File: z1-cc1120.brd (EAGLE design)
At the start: 100 x 50 mm, 13 parts, among them X1 PN61729-S

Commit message: added CCA_STATUS
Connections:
- new net RADIO_CCA_STATUS: U$1.C42, U$2.GPIO3
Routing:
- net RADIO_CCA_STATUS: track 0.00 -> 80.4 mm, vias 0 -> 1
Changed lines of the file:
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@@
 <signal name="N$2">
+</signal>
+<signal name="RADIO_CCA_STATUS">
+<contactref element="U$2" pad="GPIO3"/>
+<contactref element="U$1" pad="C42"/>
+<wire x1="96.774" y1="18.415" x2="98.679" y2="18.415" width="0.4064" layer="1"/>
+<wire x1="98.679" y1="18.415" x2="99.187" y2="17.907" width="0.4064" layer="1"/>
+<wire x1="99.187" y1="17.907" x2="99.187" y2="9.144" width="0.4064" layer="1"/>
+<wire x1="99.187" y1="9.144" x2="98.171" y2="8.128" width="0.4064" layer="1"/>
+<wire x1="98.171" y1="8.128" x2="48.133" y2="8.128" width="0.4064" layer="1"/>
+<wire x1="48.133" y1="8.128" x2="47.244" y2="9.017" width="0.4064" layer="1"/>
+<via x="47.244" y="9.017" extent="1-16" drill="0.4826"/>
+<wire x1="47.244" y1="9.017" x2="46.228" y2="10.033" width="0.4064" layer="16"/>
+<wire x1="46.228" y1="10.033" x2="39.497" y2="10.033" width="0.4064" layer="16"/>
+<wire x1="39.497" y1="10.033" x2="36.83" y2="12.7" width="0.4064" layer="16"/>
+<wire x1="36.83" y1="12.7" x2="36.83" y2="17.018" width="0.4064" layer="16"/>
 </signal>
 </signals>

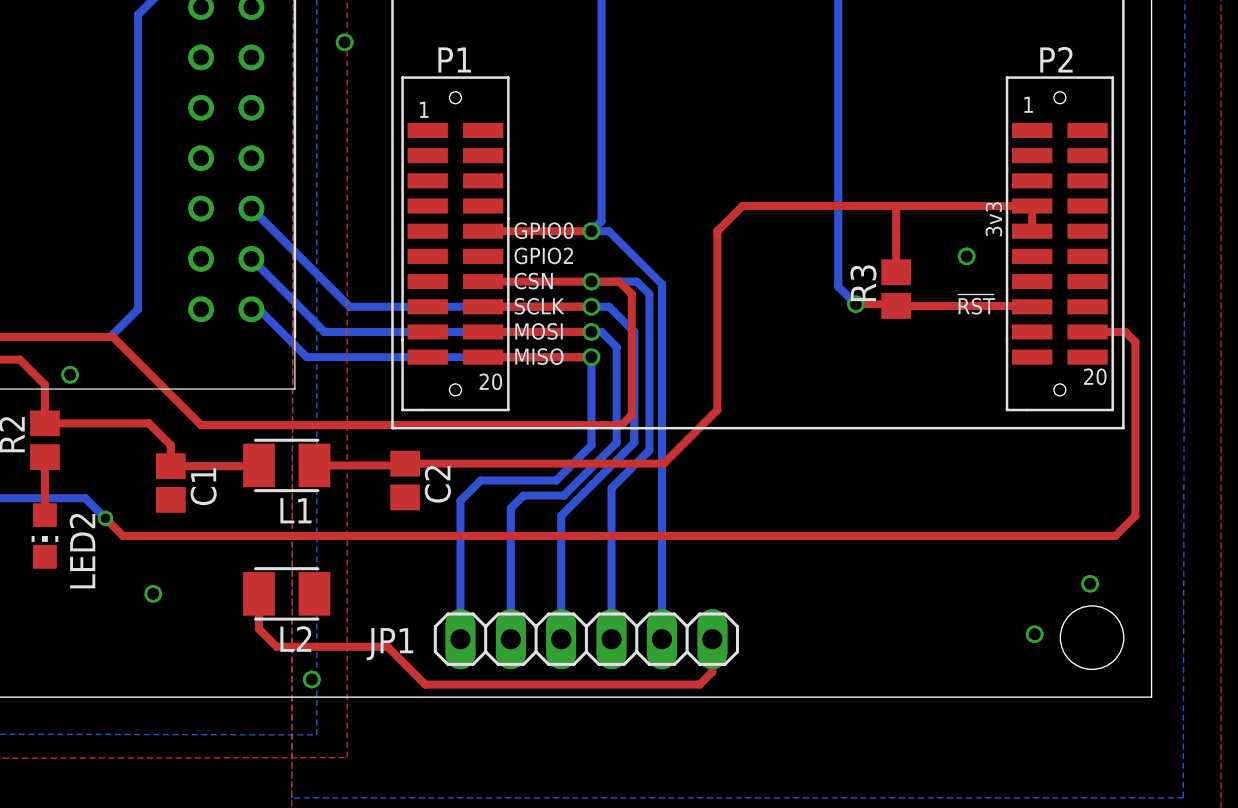
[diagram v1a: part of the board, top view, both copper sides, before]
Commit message: added !rst and cca status onto debug header
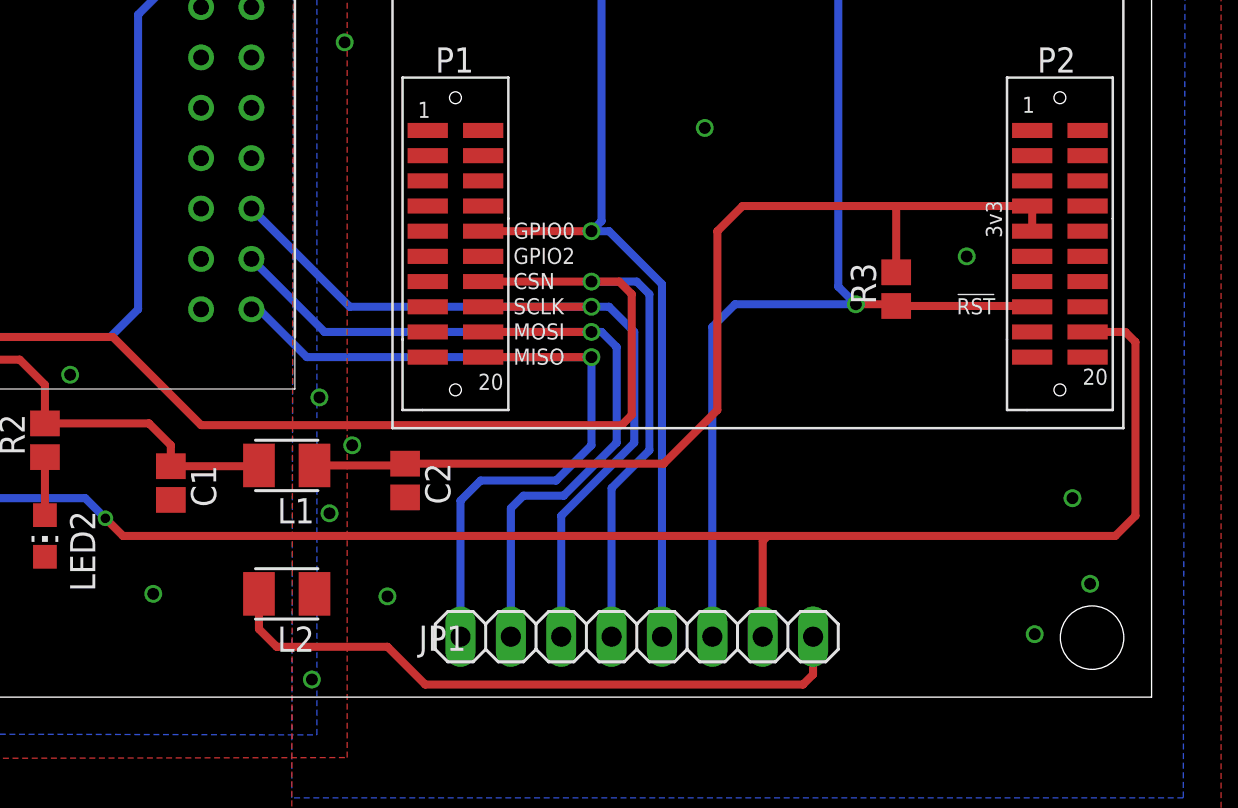
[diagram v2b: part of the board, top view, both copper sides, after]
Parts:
- JP1: device pinhead:1X06 -> pinhead:1X08
- moved JP1 2.54 mm to (74.0, 3.05)
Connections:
- net GND: now also JP1.8; no longer JP1.6
- net RADIO_!RST: now also JP1.6
- net RADIO_CCA_STATUS: now also JP1.7
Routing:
- net RADIO_!RST: track 94.9 -> 118.2 mm
- net GND: track 27.7 -> 33.0 mm
- net RADIO_CCA_STATUS: track 80.4 -> 85.6 mm
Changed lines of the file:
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@@
 <element name="L1" library="resistor" package="L3230M" value="10mH" x="56.388" y="11.684" rot="R180"/>
 <element name="L2" library="resistor" package="L3230M" value="10mH" x="56.388" y="5.207" rot="R180"/>
-<element name="JP1" library="pinhead" package="1X06" value="" x="71.501" y="2.921" smashed="yes">
-<attribute name="NAME" x="60.5028" y="2.2098" size="1.27" layer="25" ratio="10"/>
-<attribute name="VALUE" x="63.881" y="-0.254" size="1.27" layer="27"/>
+<element name="JP1" library="pinhead" package="1X08" value="" x="74.041" y="3.048" smashed="yes">
+<attribute name="NAME" x="63.0428" y="2.3368" size="1.27" layer="25" ratio="10"/>
+<attribute name="VALUE" x="66.421" y="-0.127" size="1.27" layer="27"/>
 </element>
 <element name="R3" library="resistor" package="R0805" value="1K" x="87.122" y="20.574" rot="R90"/>
@@
 <contactref element="L2" pad="2"/>
 <via x="45.466" y="16.256" extent="1-16" drill="0.6" shape="octagon"/>
-<contactref element="JP1" pad="6"/>
 <wire x1="54.988" y1="5.207" x2="54.988" y2="3.432" width="0.4064" layer="1"/>
 <wire x1="54.988" y1="3.432" x2="55.88" y2="2.54" width="0.4064" layer="1"/>
 <wire x1="55.88" y1="2.54" x2="61.468" y2="2.54" width="0.4064" layer="1"/>
 <wire x1="61.468" y1="2.54" x2="63.373" y2="0.635" width="0.4064" layer="1"/>
-<wire x1="63.373" y1="0.635" x2="77.216" y2="0.635" width="0.4064" layer="1"/>
-<wire x1="77.216" y1="0.635" x2="77.851" y2="1.27" width="0.4064" layer="1"/>
-<wire x1="77.851" y1="1.27" x2="77.851" y2="2.921" width="0.4064" layer="1"/>
+<wire x1="63.373" y1="0.635" x2="82.423" y2="0.635" width="0.4064" layer="1"/>
 <via x="49.657" y="5.207" extent="1-16" drill="0.6" shape="octagon"/>
+<contactref element="JP1" pad="8"/>
+<wire x1="82.423" y1="0.635" x2="82.931" y2="1.143" width="0.4064" layer="1"/>
+<wire x1="82.931" y1="1.143" x2="82.931" y2="3.048" width="0.4064" layer="1"/>
 </signal>
 <signal name="VCC_3V3">
@@
 <wire x1="73.914" y1="18.415" x2="73.914" y2="12.827" width="0.4064" layer="16"/>
 <wire x1="73.914" y1="12.827" x2="70.231" y2="9.144" width="0.4064" layer="16"/>
-<wire x1="70.231" y1="9.144" x2="70.231" y2="2.921" width="0.4064" layer="16"/>
+<wire x1="70.231" y1="9.144" x2="70.231" y2="3.048" width="0.4064" layer="16"/>
 </signal>
 <signal name="SPI_SIMO">
@@
 <wire x1="70.358" y1="10.16" x2="68.326" y2="10.16" width="0.4064" layer="16"/>
 <wire x1="68.326" y1="10.16" x2="67.691" y2="9.525" width="0.4064" layer="16"/>
-<wire x1="67.691" y1="9.525" x2="67.691" y2="2.921" width="0.4064" layer="16"/>
+<wire x1="67.691" y1="9.525" x2="67.691" y2="3.048" width="0.4064" layer="16"/>
 </signal>
 <signal name="SPI_SOMI">
@@
 <wire x1="69.977" y1="10.922" x2="66.167" y2="10.922" width="0.4064" layer="16"/>
 <wire x1="66.167" y1="10.922" x2="65.151" y2="9.906" width="0.4064" layer="16"/>
-<wire x1="65.151" y1="9.906" x2="65.151" y2="2.921" width="0.4064" layer="16"/>
+<wire x1="65.151" y1="9.906" x2="65.151" y2="3.048" width="0.4064" layer="16"/>
 </signal>
 <signal name="RADIO_CSN">
@@
 <wire x1="52.07" y1="13.716" x2="47.625" y2="18.161" width="0.4064" layer="1"/>
 <contactref element="JP1" pad="4"/>
-<wire x1="72.771" y1="2.921" x2="72.771" y2="10.541" width="0.4064" layer="16"/>
+<wire x1="72.771" y1="3.048" x2="72.771" y2="10.541" width="0.4064" layer="16"/>
 <wire x1="72.771" y1="10.541" x2="74.676" y2="12.446" width="0.4064" layer="16"/>
 <wire x1="74.676" y1="12.446" x2="74.676" y2="20.32" width="0.4064" layer="16"/>
@@
 <wire x1="71.755" y1="23.495" x2="72.644" y2="23.495" width="0.4064" layer="16"/>
 <wire x1="72.644" y1="23.495" x2="75.311" y2="20.828" width="0.4064" layer="16"/>
-<wire x1="75.311" y1="20.828" x2="75.311" y2="2.921" width="0.4064" layer="16"/>
+<wire x1="75.311" y1="20.828" x2="75.311" y2="3.048" width="0.4064" layer="16"/>
 <contactref element="U$1" pad="C54"/>
 <wire x1="47.498" y1="18.161" x2="22.733" y2="18.161" width="0.4064" layer="16"/>
@@
 <via x="59.309" y="33.02" extent="1-16" drill="0.6"/>
 <via x="90.678" y="22.225" extent="1-16" drill="0.6"/>
+<via x="61.468" y="5.08" extent="1-16" drill="0.6" shape="octagon"/>
+<via x="96.012" y="10.033" extent="1-16" drill="0.6" shape="octagon"/>
+<via x="58.547" y="9.271" extent="1-16" drill="0.6" shape="octagon"/>
+<via x="58.039" y="15.113" extent="1-16" drill="0.6" shape="octagon"/>
+<via x="59.69" y="12.7" extent="1-16" drill="0.6" shape="octagon"/>
+<via x="77.47" y="28.702" extent="1-16" drill="0.6" shape="octagon"/>
 </signal>
 <signal name="RADIO_3V3">
@@
 <wire x1="87.122" y1="19.724" x2="87.034" y2="19.724" width="0.4064" layer="1"/>
 <wire x1="87.034" y1="19.724" x2="87.034" y2="19.812" width="0.4064" layer="1"/>
+<contactref element="JP1" pad="6"/>
+<wire x1="85.09" y1="19.812" x2="78.994" y2="19.812" width="0.4064" layer="16"/>
+<wire x1="78.994" y1="19.812" x2="77.851" y2="18.669" width="0.4064" layer="16"/>
+<wire x1="77.851" y1="18.669" x2="77.851" y2="3.048" width="0.4064" layer="16"/>
 </signal>
 <signal name="N$2">
@@
 <wire x1="99.187" y1="17.907" x2="99.187" y2="9.144" width="0.4064" layer="1"/>
 <wire x1="99.187" y1="9.144" x2="98.171" y2="8.128" width="0.4064" layer="1"/>
-<wire x1="98.171" y1="8.128" x2="48.133" y2="8.128" width="0.4064" layer="1"/>
+<wire x1="98.171" y1="8.128" x2="80.645" y2="8.128" width="0.4064" layer="1"/>
+<wire x1="80.645" y1="8.128" x2="48.133" y2="8.128" width="0.4064" layer="1"/>
 <wire x1="48.133" y1="8.128" x2="47.244" y2="9.017" width="0.4064" layer="1"/>
 <via x="47.244" y="9.017" extent="1-16" drill="0.4826"/>
@@
 <wire x1="39.497" y1="10.033" x2="36.83" y2="12.7" width="0.4064" layer="16"/>
 <wire x1="36.83" y1="12.7" x2="36.83" y2="17.018" width="0.4064" layer="16"/>
+<contactref element="JP1" pad="7"/>
+<wire x1="80.391" y1="3.048" x2="80.391" y2="7.874" width="0.4064" layer="1"/>
+<wire x1="80.391" y1="7.874" x2="80.645" y2="8.128" width="0.4064" layer="1"/>
 </signal>
 </signals>

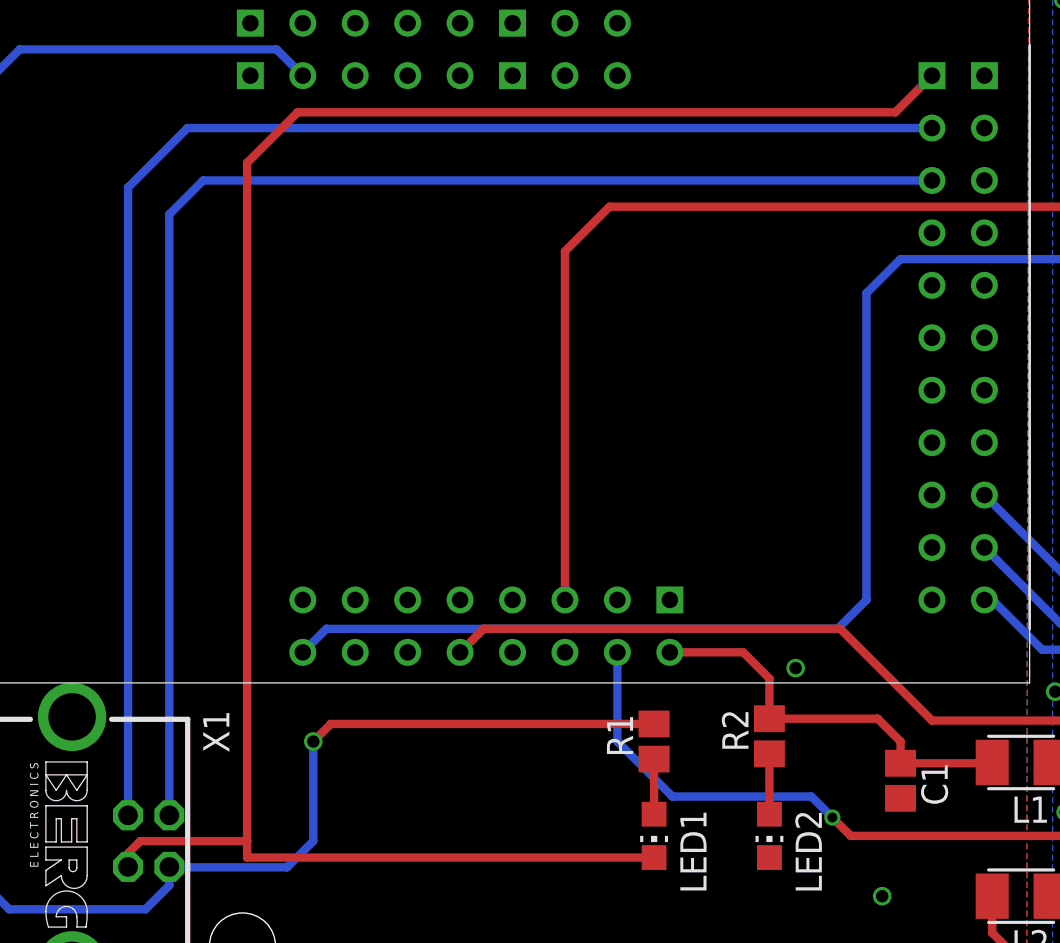
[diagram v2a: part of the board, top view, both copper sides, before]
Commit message: now very similar length usb tracks
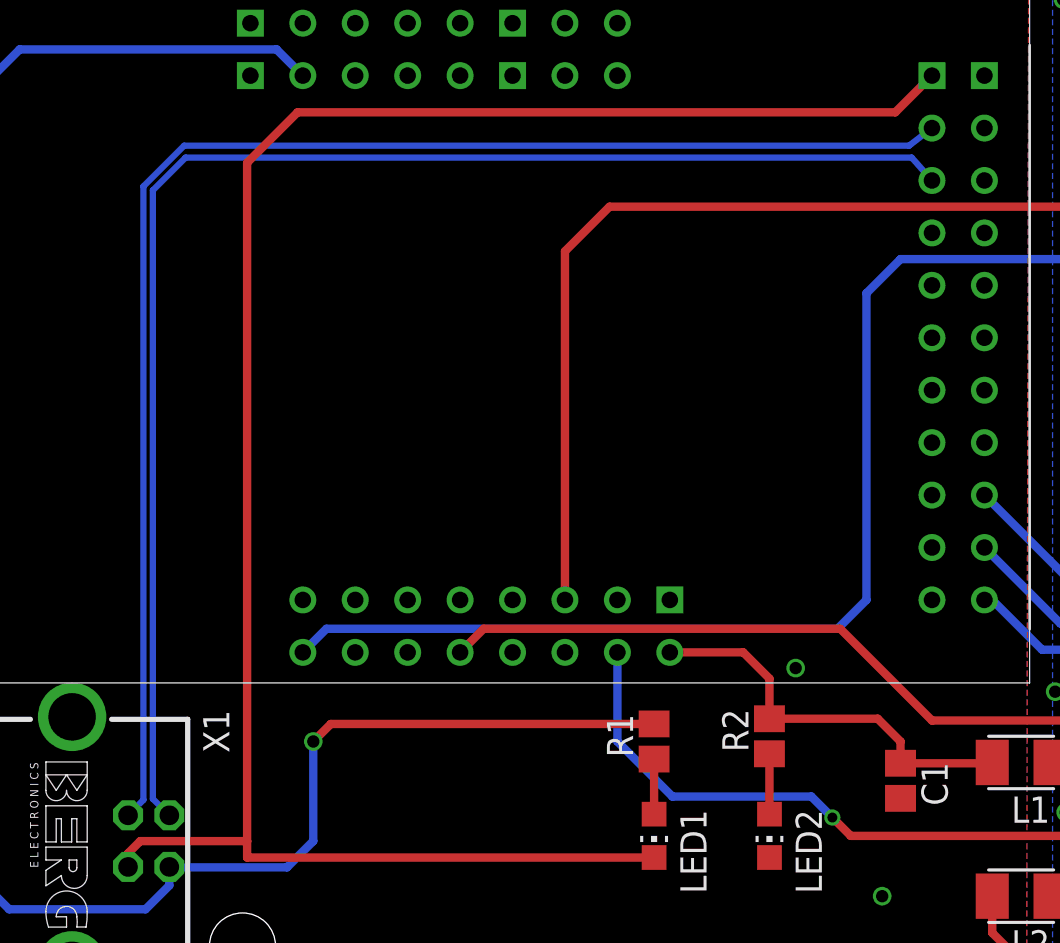
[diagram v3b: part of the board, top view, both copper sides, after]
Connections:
- net USB_D+ renamed USB_P
- net USB_D- renamed USB_N
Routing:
- net USB_N: track 66.7 -> 69.5 mm
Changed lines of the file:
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@@
 <class number="0" name="default" width="0" drill="0">
+</class>
+<class number="1" name="usb" width="0.3048" drill="0">
+<clearance class="1" value="0.1524"/>
 </class>
 </classes>
@@
 <wire x1="15.144" y1="6.604" x2="15.124" y2="6.624" width="0.4064" layer="16"/>
 </signal>
-<signal name="USB_D+">
+<signal name="USB_P" class="1">
 <contactref element="U$1" pad="B19"/>
 <contactref element="X1" pad="3"/>
-<wire x1="13.124" y1="9.124" x2="13.124" y2="39.54" width="0.4064" layer="16"/>
-<wire x1="13.124" y1="39.54" x2="16.002" y2="42.418" width="0.4064" layer="16"/>
-<wire x1="16.002" y1="42.418" x2="52.07" y2="42.418" width="0.4064" layer="16"/>
-</signal>
-<signal name="USB_D-">
+<wire x1="13.124" y1="9.124" x2="13.8684" y2="9.8684" width="0.3048" layer="16"/>
+<wire x1="13.8684" y1="9.8684" x2="13.8684" y2="39.59169375" width="0.3048" layer="16"/>
+<wire x1="13.8684" y1="39.59169375" x2="15.840353125" y2="41.563646875" width="0.3048" layer="16"/>
+<wire x1="15.840353125" y1="41.563646875" x2="50.961646875" y2="41.563646875" width="0.3048" layer="16"/>
+<wire x1="50.961646875" y1="41.563646875" x2="52.07" y2="42.418" width="0.3048" layer="16"/>
+</signal>
+<signal name="USB_N" class="1">
 <contactref element="U$1" pad="B21"/>
 <contactref element="X1" pad="2"/>
-<wire x1="15.124" y1="9.124" x2="15.124" y2="38.238" width="0.4064" layer="16"/>
-<wire x1="15.124" y1="38.238" x2="16.764" y2="39.878" width="0.4064" layer="16"/>
-<wire x1="16.764" y1="39.878" x2="52.07" y2="39.878" width="0.4064" layer="16"/>
+<wire x1="15.124" y1="9.124" x2="14.3256" y2="9.9224" width="0.3048" layer="16"/>
+<wire x1="14.3256" y1="9.9224" x2="14.3256" y2="39.40230625" width="0.3048" layer="16"/>
+<wire x1="14.3256" y1="39.40230625" x2="15.909646875" y2="40.986353125" width="0.3048" layer="16"/>
+<wire x1="15.909646875" y1="40.986353125" x2="51.088646875" y2="40.986353125" width="0.3048" layer="16"/>
+<wire x1="51.088646875" y1="40.986353125" x2="52.07" y2="39.878" width="0.3048" layer="16"/>
 </signal>
 <signal name="USB_GND">
